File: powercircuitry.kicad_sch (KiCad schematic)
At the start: 150 parts, among them U4001 TPS6521903RHBR, U4002 AM6231ASGGGAALW, U4003 TLV62592DMQR

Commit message: Fixed ERC errors and warnings (zero errors and zero warnings)
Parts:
- added R4014: R, symbol Device:R
- added R4015: 10k, symbol Device:R
- renumbered C4119 to C4118, C4118 to C4119, U4002 to U1001
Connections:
- net VDDR_CORE is gone; now on net VDDA_0V85: C4012.1, U4001.19 (VLDO2)
- net GND: now also R4015.2
- net VDD_1V8: now also R4014.1
- net VPP_1V8: no longer names the net of U1001.J8 (VPP)
- net VPP_1V8: now also R4014.2, R4015.1
- no-connect marks 2 -> 3

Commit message: Labeled all nets and added some footprints
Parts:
- U1001: footprint (none) -> AM6231ASGGGAALW:BGA425C50P25X25_1300X1300X89
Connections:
- net VDD_3V3_FB: now reaches C4018.1, R4011.1, R4013.1, U4003.3 (FB)
- net CAP_VDDS_MCU: now reaches C4028.1, U1001.H11 (CAP_VDDS_MCU)
- net PMIC_B1_FB: now reaches R4001.1, U4001.1 (FB_B1)
- net PMIC_B1_O: now reaches L4001.1, U4001.2 (LX_B1_1), U4001.3 (LX_B1_2)
- net PMIC_B3_O: now reaches L4003.1, U4001.27 (LX_B3)
- net PMIC_B2_O: now reaches L4002.1, U4001.29 (LX_B2)
- net CAP_VDDS6: now reaches C4027.1, U1001.J19 (CAP_VDDS6)
- net VDD_3V3_PG: now reaches R4009.2, U4003.2 (PG)
- net VDD_3V3_SW: now reaches L4004.1, U4003.5 (SW)
- net SoC_VPP: now reaches R4014.2, R4015.1, U1001.J8 (VPP)
- net CAP_VDDS1: now reaches C4022.1, U1001.K18 (CAP_VDDS1)
- net CAP_VDDS5: now reaches C4026.1, U1001.H17 (CAP_VDDS5)
- net CAP_VDDS3: now reaches C4024.1, U1001.P19 (CAP_VDDS3)
- net CAP_VDDS2: now reaches C4023.1, U1001.W17 (CAP_VDDS2)
- net CAP_VDDS4: now reaches C4025.1, U1001.U7 (CAP_VDDS4)
- net CAP_VDDS_CANUART: now reaches C4029.1, U1001.G9 (CAP_VDDS_CANUART)
- net CAP_VDDS0: now reaches C4021.1, U1001.H15 (CAP_VDDS0)
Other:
- moved on the sheet: L4004, U1001B

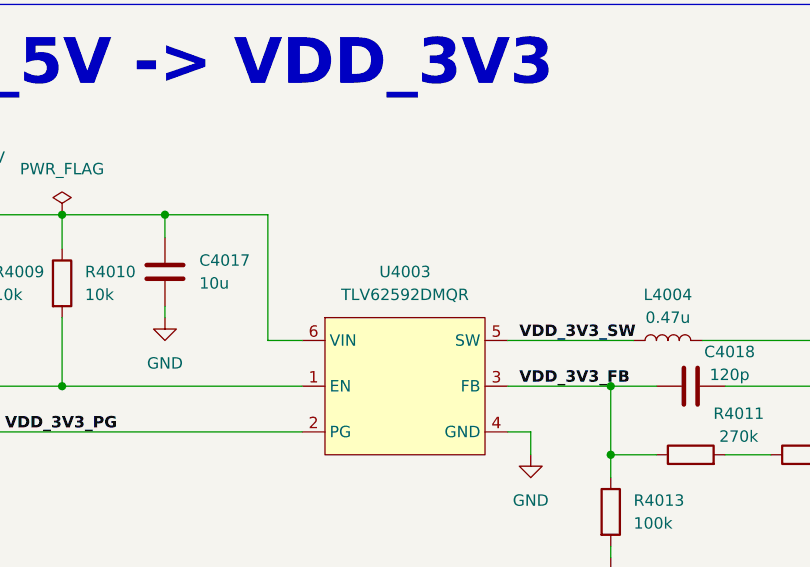
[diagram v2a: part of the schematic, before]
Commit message: Added some footprints for important ICs
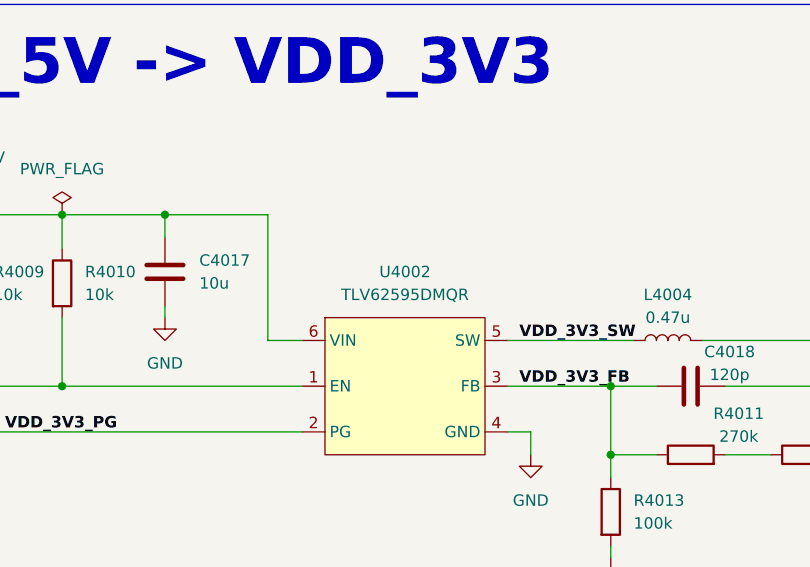
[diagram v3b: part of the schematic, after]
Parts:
- removed U4003: TLV62592DMQR, symbol SoftServicesSymbolLibrary:TLV62592DMQR
- added U4002: TLV62595DMQR, SoftServicesFootprintLibrary:TLV62595DMQR, symbol SoftServicesSymbolLibrary:TLV62595DMQR
- U4001: footprint (none) -> TPS6521903RHBR:QFN50P500X500X100-33N-D
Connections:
- net GND: now also U4002.4 (GND)
- net VDD_3V3_EN: now also U4002.1 (EN)
- net VDD_3V3_FB: now also U4002.3 (FB)
- net VDD_3V3_PG: now also U4002.2 (PG)
- net VDD_3V3_SW: now also U4002.5 (SW)
- net VSYS_5V: now also U4002.6 (VIN)
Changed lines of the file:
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@@
 			)
 		)
-		(property "Footprint" ""
+		(property "Footprint" "TPS6521903RHBR:QFN50P500X500X100-33N-D"
 			(at 156.21 124.46 0)
 			(effects
@@
 	)
 	(symbol
-		(lib_id "SoftServicesSymbolLibrary:TLV62592DMQR")
-		(at 97.79 243.84 0)
-		(unit 1)
-		(exclude_from_sim no)
-		(in_bom yes)
-		(on_board yes)
-		(dnp no)
-		(fields_autoplaced yes)
-		(property "Reference" "U4003"
-			(at 97.79 232.41 0)
-			(effects
-				(font
-					(size 1.27 1.27)
-				)
-			)
-		)
-		(property "Value" "TLV62592DMQR"
-			(at 97.79 234.95 0)
-			(effects
-				(font
-					(size 1.27 1.27)
-				)
-			)
-		)
-		(property "Footprint" ""
-			(at 97.79 243.84 0)
-			(effects
-				(font
-					(size 1.27 1.27)
-				)
-				(hide yes)
-			)
-		)
-		(property "Datasheet" ""
-			(at 97.79 243.84 0)
-			(effects
-				(font
-					(size 1.27 1.27)
-				)
-				(hide yes)
-			)
-		)
-		(property "Description" ""
-			(at 97.79 243.84 0)
-			(effects
-				(font
-					(size 1.27 1.27)
-				)
-				(hide yes)
-			)
-		)
-		(pin "5"
-		)
-		(pin "2"
-		)
-		(pin "6"
-		)
-		(pin "4"
-		)
-		(pin "1"
-		)
-		(pin "3"
-		)
-		(instances
-			(project ""
-				(path "/b43b7bca-e50d-42ec-8ff0-e0016dfefe0a/13a7821e-2ee3-4360-911d-96166c961e5a"
-					(reference "U4003")
-					(unit 1)
-				)
-			)
-		)
-	)
-	(symbol
 		(lib_id "power:VDD")
 		(at 378.46 544.83 0)
@@
 					(unit 1)
 				)
+			)
+		)
+	)
+	(symbol
+		(lib_id "SoftServicesSymbolLibrary:TLV62595DMQR")
+		(at 97.79 243.84 0)
+		(unit 1)
+		(exclude_from_sim no)
+		(in_bom yes)
+		(on_board yes)
+		(dnp no)
+		(fields_autoplaced yes)
+		(property "Reference" "U4002"
+			(at 97.79 232.41 0)
+			(effects
+				(font
+					(size 1.27 1.27)
+				)
+			)
+		)
+		(property "Value" "TLV62595DMQR"
+			(at 97.79 234.95 0)
+			(effects
+				(font
+					(size 1.27 1.27)
+				)
+			)
+		)
+		(property "Footprint" "SoftServicesFootprintLibrary:TLV62595DMQR"
+			(at 97.79 243.84 0)
+			(effects
+				(font
+					(size 1.27 1.27)
+				)
+				(hide yes)
+			)
+		)
+		(property "Datasheet" ""
+			(at 97.79 243.84 0)
+			(effects
+				(font
+					(size 1.27 1.27)
+				)
+				(hide yes)
+			)
+		)
+		(property "Description" ""
+			(at 97.79 243.84 0)
+			(effects
+				(font
+					(size 1.27 1.27)
+				)
+				(hide yes)
+			)
+		)
+		(pin "2"
+		)
+		(pin "6"
+		)
+		(pin "5"
+		)
+		(pin "1"
+		)
+		(pin "4"
+		)
+		(pin "3"
+		)
+		(instances
+			(project ""
+				(path "/b43b7bca-e50d-42ec-8ff0-e0016dfefe0a/13a7821e-2ee3-4360-911d-96166c961e5a"
+					(reference "U4002")
+					(unit 1)
+				)

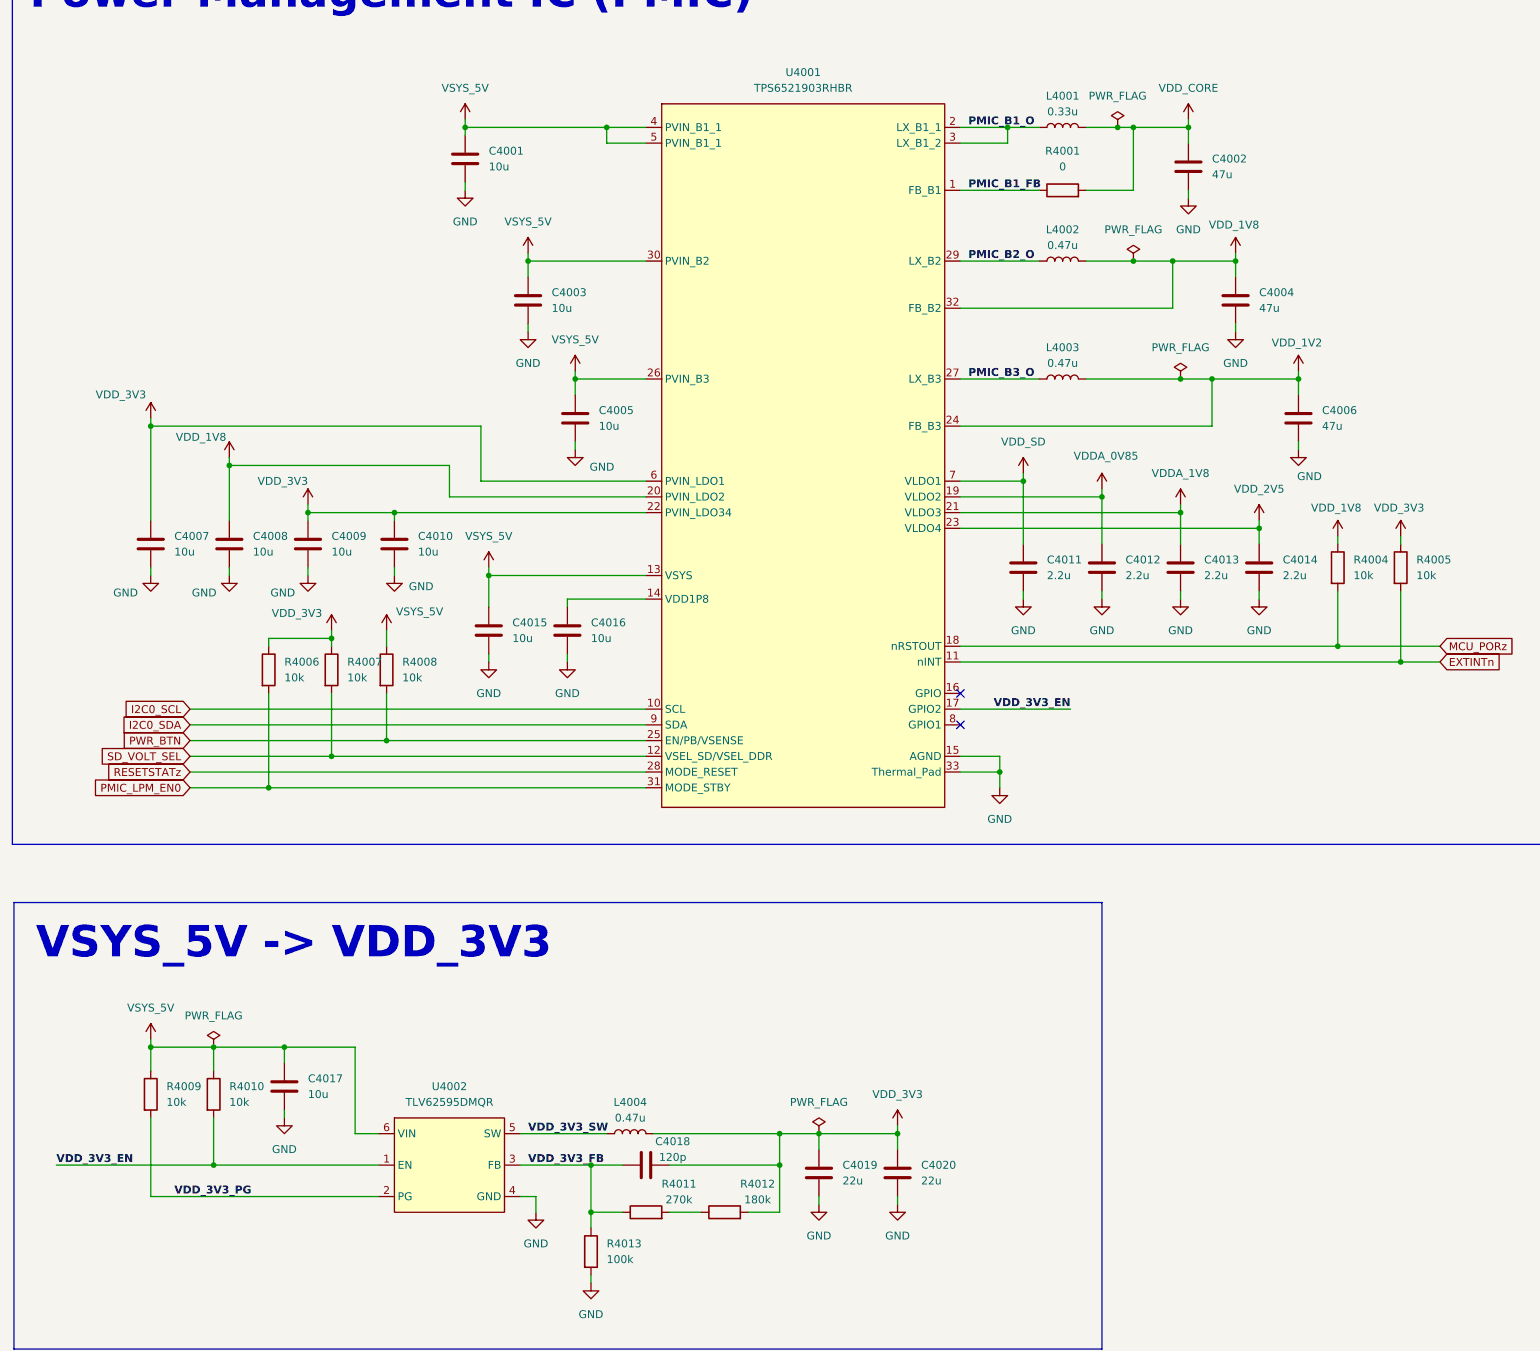
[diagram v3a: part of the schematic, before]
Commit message: Double checked power, ddr4, USB, MMC and added bootstrap. Also added buttons and added pinmuxing in sysconfig
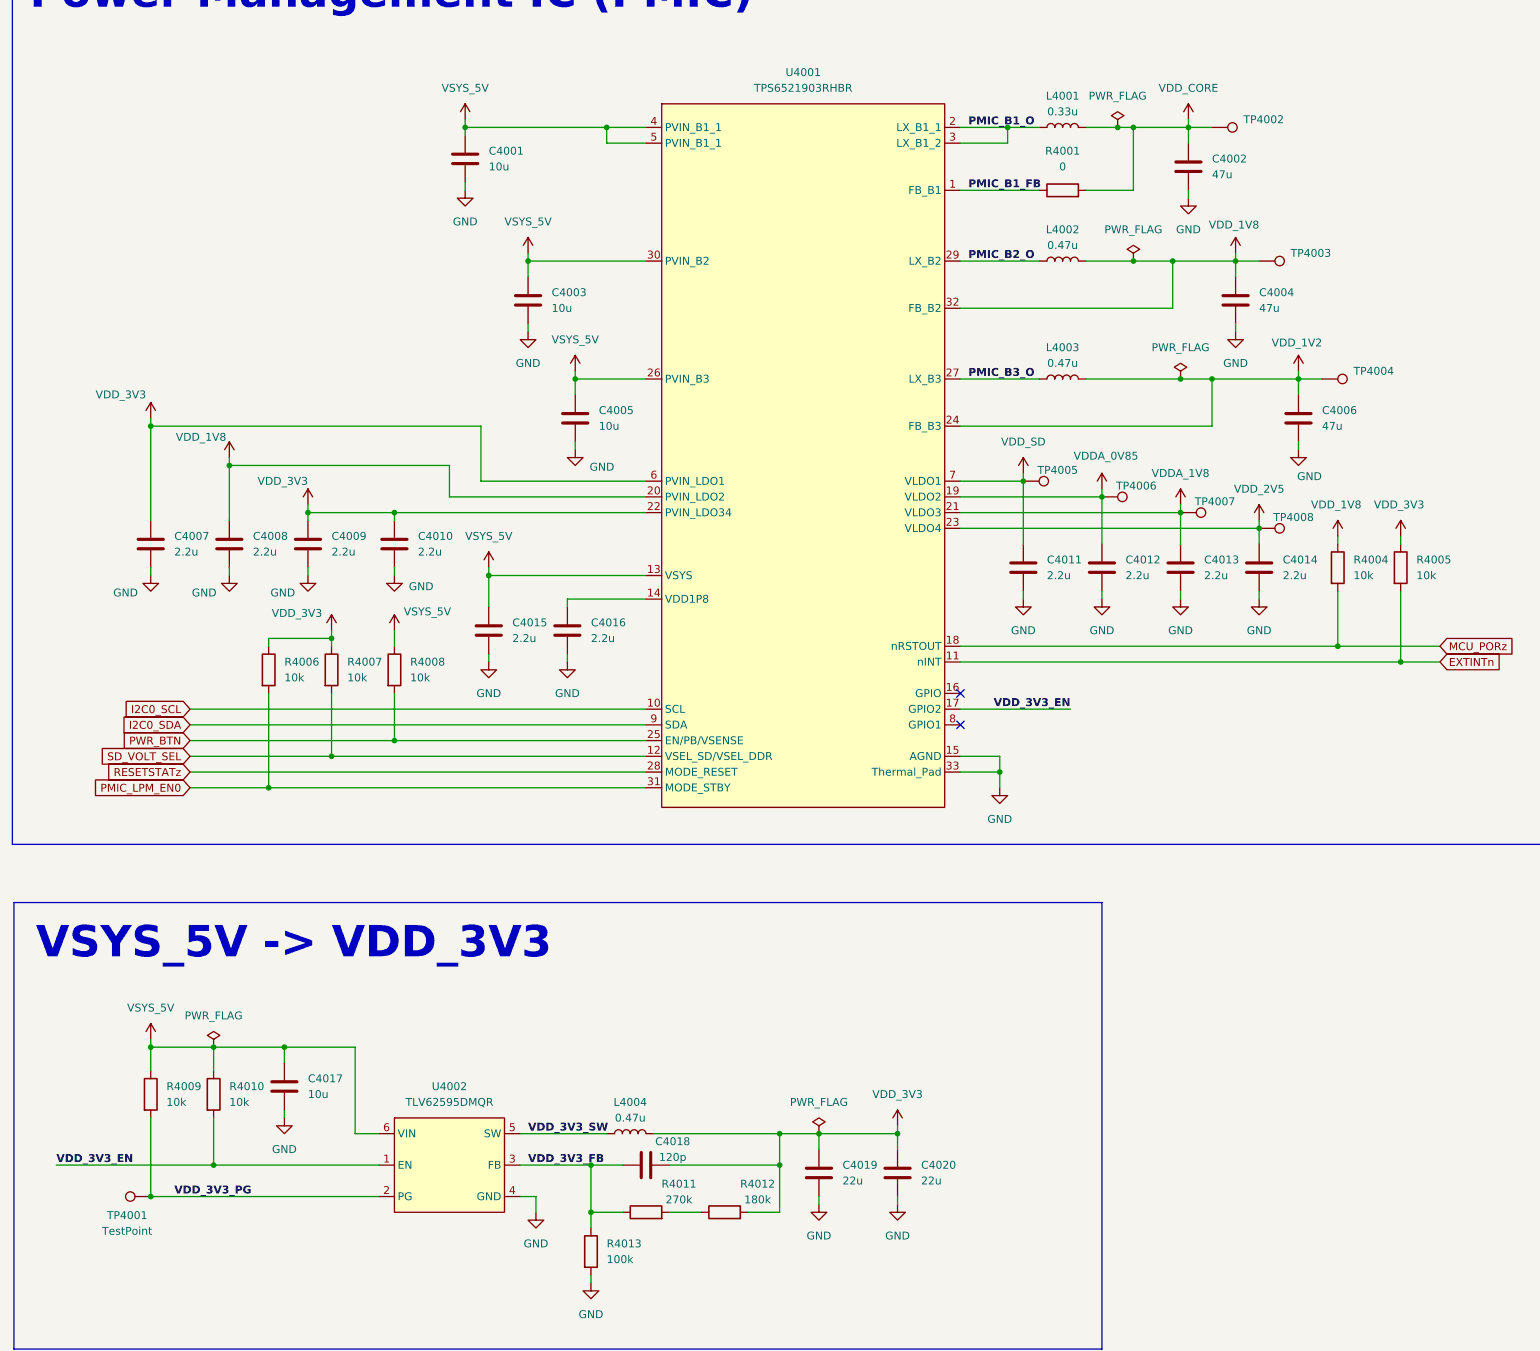
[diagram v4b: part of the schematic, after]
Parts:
- added TP4001, TP4002, TP4003, TP4004, TP4005, TP4006, TP4007, TP4008: TestPoint, symbol Connector:TestPoint
- C4007, C4008, C4009, C4010, C4015, C4016: value 10u -> 2.2u
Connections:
- net VDDA_0V85: now also TP4006.1
- net VDDA_1V8: now also TP4007.1
- net VDD_1V2: now also TP4004.1
- net VDD_1V8: now also TP4003.1
- net VDD_2V5: now also TP4008.1
- net VDD_3V3_PG: now also TP4001.1
- net VDD_CORE: now also TP4002.1
- net VDD_SD: now also TP4005.1
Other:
- moved on the sheet: R4008

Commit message: Added capcitor footprints
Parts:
- C4001, C4003, C4005, C4017: footprint (none) -> Capacitor_SMD:C_0603_1608Metric
- C4002, C4004, C4006, C4019, C4020: footprint (none) -> Capacitor_SMD:C_0805_2012Metric
- C4007, C4008, C4009, C4010, C4011, C4012, C4013, C4014, C4015, C4016, C4018, C4030, C4031, C4049, C4050, C4059, C4071, C4080, C4081, C4088, C4094, C4097, C4103, C4112: footprint (none) -> Capacitor_SMD:C_0402_1005Metric
- C4021, C4022, C4023, C4024, C4025, C4026, C4027, C4028, C4029, C4032, C4033, C4034, C4035, C4036, C4037, C4038, C4039, C4040, C4041, C4042, C4043, C4044, C4045, C4046, C4047, C4048, C4051, C4052, C4053, C4054, C4055, C4056, C4057, C4058, C4060, C4061, C4062, C4063, C4064, C4065, C4066, C4067, C4068, C4069, C4070, C4072, C4073, C4074, C4075, C4076, C4077, C4078, C4079, C4082, C4083, C4084, C4085, C4086, C4087, C4089, C4090, C4091, C4092, C4093, C4095, C4096, C4098, C4099, C4100, C4101, C4102, C4104, C4105, C4106, C4107, C4108, C4109, C4110, C4111, C4113, C4114, C4115, C4116, C4117, C4118, C4119: footprint (none) -> Capacitor_SMD:C_0201_0603Metric
